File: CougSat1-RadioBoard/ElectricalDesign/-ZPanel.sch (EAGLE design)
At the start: 47 parts, among them J1 High Gain Antenna, J2 Deployables, J3 High Gain +, J4 ADCS, J5 Flap +X, J6 Flap -X, J7 Flap +Y, J8 Flap -Y, U1 AD7291, U3 AD8515

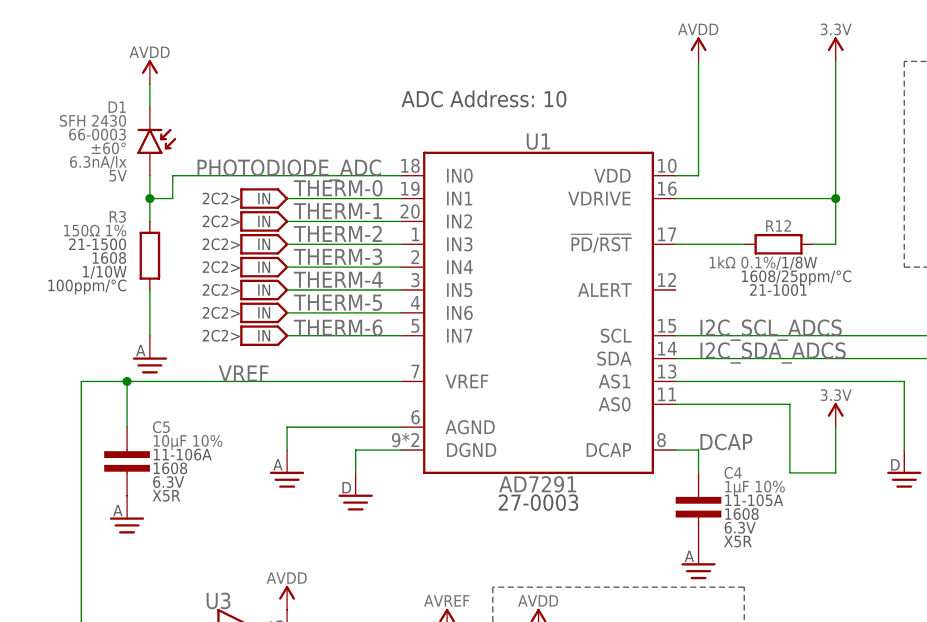
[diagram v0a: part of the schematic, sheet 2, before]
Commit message: Ready for re-review
Fixed issues mentioned before.
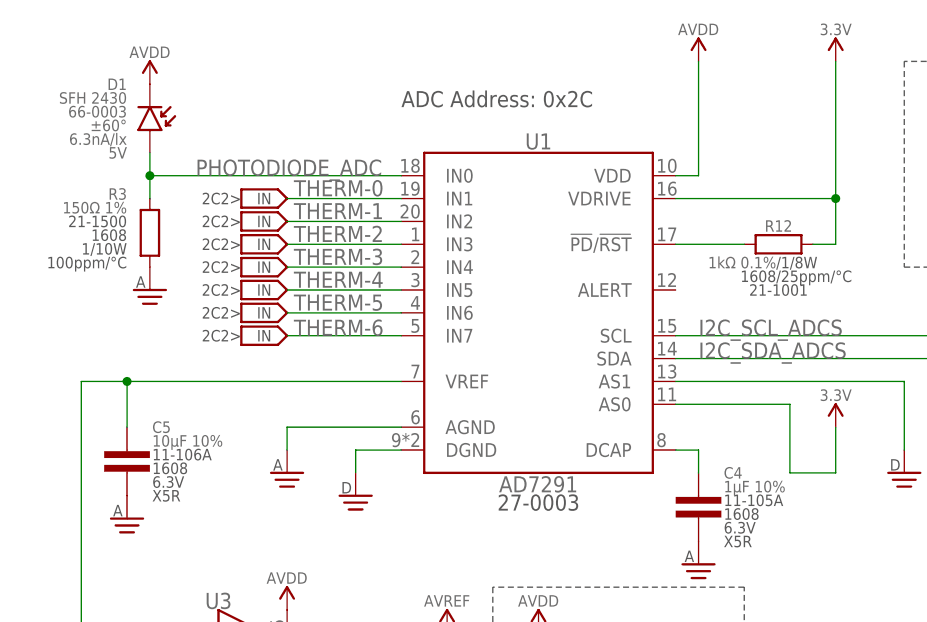
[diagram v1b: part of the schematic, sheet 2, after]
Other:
- note added: "ADC Address: 0x2C"
- note removed: "ADC Address: 10"
- moved on the sheet: D1, R3
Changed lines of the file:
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@@
 <wire x1="78.74" y1="106.68" x2="78.74" y2="129.54" width="0.1524" layer="97" style="shortdash"/>
 <wire x1="78.74" y1="129.54" x2="50.8" y2="129.54" width="0.1524" layer="97" style="shortdash"/>
-<text x="40.64" y="182.88" size="1.778" layer="97">ADC Address: 10</text>
+<text x="40.64" y="182.88" size="1.778" layer="97">ADC Address: 0x2C</text>
 </plain>
 <instances>
@@
 <attribute name="PACKAGE" x="11.557" y="63.754" size="1.778" layer="97" align="center"/>
 </instance>
-<instance part="D1" gate="G$1" x="12.7" y="180.34" smashed="yes" rot="R180">
-<attribute name="NAME" x="10.16" y="182.88" size="1.27" layer="95" rot="R180" align="center-left"/>
-<attribute name="VALUE" x="10.16" y="181.356" size="1.27" layer="95" rot="R180" align="center-left"/>
-<attribute name="SKU" x="10.16" y="179.832" size="1.27" layer="95" rot="R180" align="center-left"/>
-<attribute name="SENSITIVITY" x="10.16" y="176.784" size="1.27" layer="95" rot="R180" align="center-left"/>
-<attribute name="VR" x="10.16" y="175.26" size="1.27" layer="95" rot="R180" align="center-left"/>
-<attribute name="HALF_ANGLE" x="10.16" y="178.308" size="1.27" layer="95" rot="R180" align="center-left"/>
-</instance>
-<instance part="R3" gate="G$1" x="12.7" y="165.1" smashed="yes" rot="MR0">
-<attribute name="NAME" x="10.16" y="170.688" size="1.27" layer="95" rot="MR0" align="center-left"/>
-<attribute name="VALUE" x="10.16" y="169.164" size="1.27" layer="96" rot="MR0" align="center-left"/>
-<attribute name="PACKAGE" x="10.16" y="166.116" size="1.27" layer="97" rot="MR0" align="center-left"/>
-<attribute name="POWER" x="10.16" y="164.592" size="1.27" layer="97" rot="MR0" align="center-left"/>
-<attribute name="TEMP" x="10.16" y="163.068" size="1.27" layer="97" rot="MR0" align="center-left"/>
-<attribute name="SKU" x="10.16" y="167.64" size="1.27" layer="97" rot="MR0" align="center-left"/>
-</instance>
-<instance part="SUPPLY1" gate="G$1" x="12.7" y="154.94" smashed="yes"/>
+<instance part="D1" gate="G$1" x="12.7" y="182.88" smashed="yes" rot="R180">
+<attribute name="NAME" x="10.16" y="185.42" size="1.27" layer="95" rot="R180" align="center-left"/>
+<attribute name="VALUE" x="10.16" y="183.896" size="1.27" layer="95" rot="R180" align="center-left"/>
+<attribute name="SKU" x="10.16" y="182.372" size="1.27" layer="95" rot="R180" align="center-left"/>
+<attribute name="SENSITIVITY" x="10.16" y="179.324" size="1.27" layer="95" rot="R180" align="center-left"/>
+<attribute name="VR" x="10.16" y="177.8" size="1.27" layer="95" rot="R180" align="center-left"/>
+<attribute name="HALF_ANGLE" x="10.16" y="180.848" size="1.27" layer="95" rot="R180" align="center-left"/>
+</instance>
+<instance part="R3" gate="G$1" x="12.7" y="167.64" smashed="yes" rot="MR0">
+<attribute name="NAME" x="10.16" y="173.228" size="1.27" layer="95" rot="MR0" align="center-left"/>
+<attribute name="VALUE" x="10.16" y="171.704" size="1.27" layer="96" rot="MR0" align="center-left"/>
+<attribute name="PACKAGE" x="10.16" y="168.656" size="1.27" layer="97" rot="MR0" align="center-left"/>
+<attribute name="POWER" x="10.16" y="167.132" size="1.27" layer="97" rot="MR0" align="center-left"/>
+<attribute name="TEMP" x="10.16" y="165.608" size="1.27" layer="97" rot="MR0" align="center-left"/>
+<attribute name="SKU" x="10.16" y="170.18" size="1.27" layer="97" rot="MR0" align="center-left"/>
+</instance>
+<instance part="SUPPLY1" gate="G$1" x="12.7" y="162.56" smashed="yes"/>
 <instance part="J3" gate="G$1" x="190.5" y="177.8" smashed="yes">
 <attribute name="VALUE" x="191.135" y="173.99" size="1.778" layer="96" align="center"/>
@@
 </net>
 <net name="AGND" class="0">
-<segment>
-<pinref part="R3" gate="G$1" pin="1"/>
-<wire x1="12.7" y1="162.56" x2="12.7" y2="157.48" width="0.1524" layer="91"/>
-<pinref part="SUPPLY1" gate="G$1" pin="AGND"/>
-</segment>
 <segment>
 <pinref part="SUPPLY16" gate="G$1" pin="AGND"/>
@@
 <pinref part="SUPPLY42" gate="G$1" pin="AGND"/>
 </segment>
+<segment>
+<pinref part="R3" gate="G$1" pin="1"/>
+<pinref part="SUPPLY1" gate="G$1" pin="AGND"/>
+</segment>
 </net>
 <net name="3.3V" class="0">
@@
 <segment>
 <pinref part="D1" gate="G$1" pin="C"/>
-<wire x1="12.7" y1="182.88" x2="12.7" y2="185.42" width="0.1524" layer="91"/>
 <pinref part="SUPPLY2" gate="G$1" pin="AVDD"/>
 </segment>
@@
 <wire x1="73.66" y1="142.24" x2="73.66" y2="144.78" width="0.1524" layer="91"/>
 <wire x1="73.66" y1="144.78" x2="71.12" y2="144.78" width="0.1524" layer="91"/>
-<label x="73.66" y="144.78" size="1.778" layer="95"/>
 </segment>
 </net>
@@
 <wire x1="10.16" y1="147.32" x2="10.16" y2="152.4" width="0.1524" layer="91"/>
 <junction x="10.16" y="152.4"/>
-<label x="20.32" y="152.4" size="1.778" layer="95"/>
 </segment>
 </net>
@@
 <segment>
 <pinref part="U1" gate="G$1" pin="IN0"/>
-<wire x1="40.64" y1="175.26" x2="15.24" y2="175.26" width="0.1524" layer="91"/>
-<wire x1="15.24" y1="175.26" x2="15.24" y2="172.72" width="0.1524" layer="91"/>
+<wire x1="40.64" y1="175.26" x2="12.7" y2="175.26" width="0.1524" layer="91"/>
+<label x="17.78" y="175.26" size="1.778" layer="95"/>
+<pinref part="D1" gate="G$1" pin="A"/>
 <pinref part="R3" gate="G$1" pin="2"/>
-<pinref part="D1" gate="G$1" pin="A"/>
-<wire x1="12.7" y1="170.18" x2="12.7" y2="172.72" width="0.1524" layer="91"/>
 <wire x1="12.7" y1="172.72" x2="12.7" y2="175.26" width="0.1524" layer="91"/>
-<wire x1="15.24" y1="172.72" x2="12.7" y2="172.72" width="0.1524" layer="91"/>
-<junction x="12.7" y="172.72"/>
-<label x="17.78" y="175.26" size="1.778" layer="95"/>
-</segment>
-</net>
+<wire x1="12.7" y1="175.26" x2="12.7" y2="177.8" width="0.1524" layer="91"/>
+<junction x="12.7" y="175.26"/>
+</segment>
+</net>

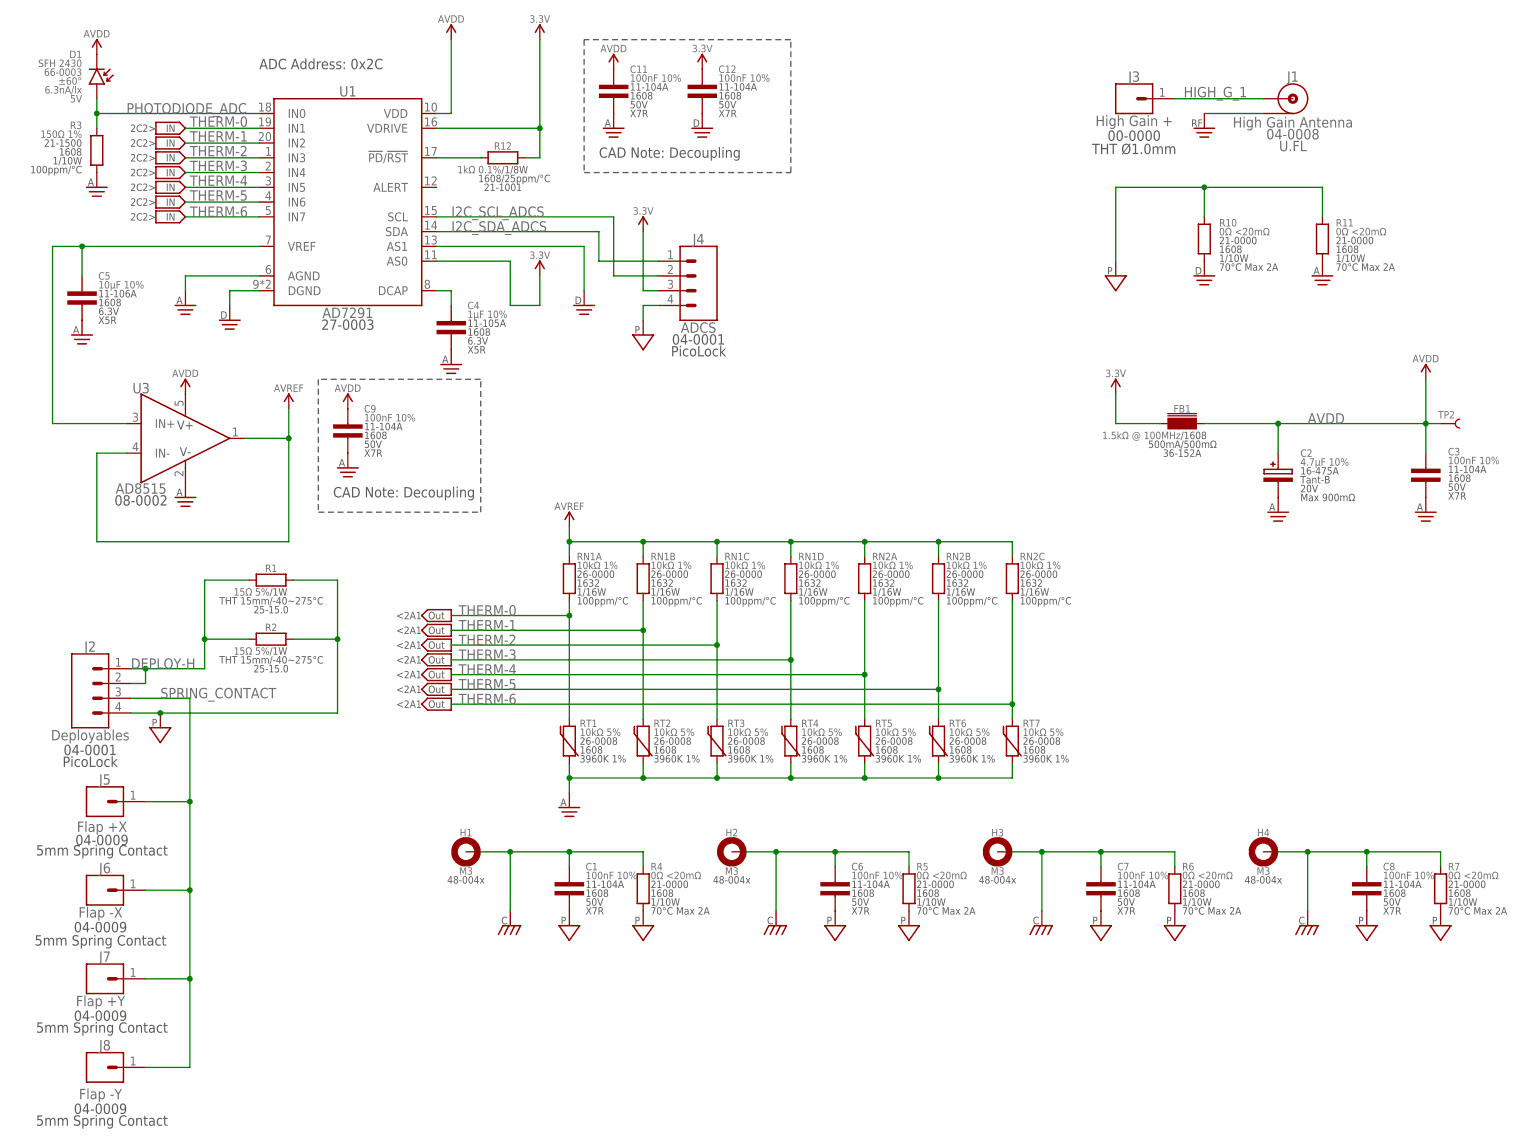
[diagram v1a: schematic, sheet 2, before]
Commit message: Fixed formatting and adjusted antenna tests
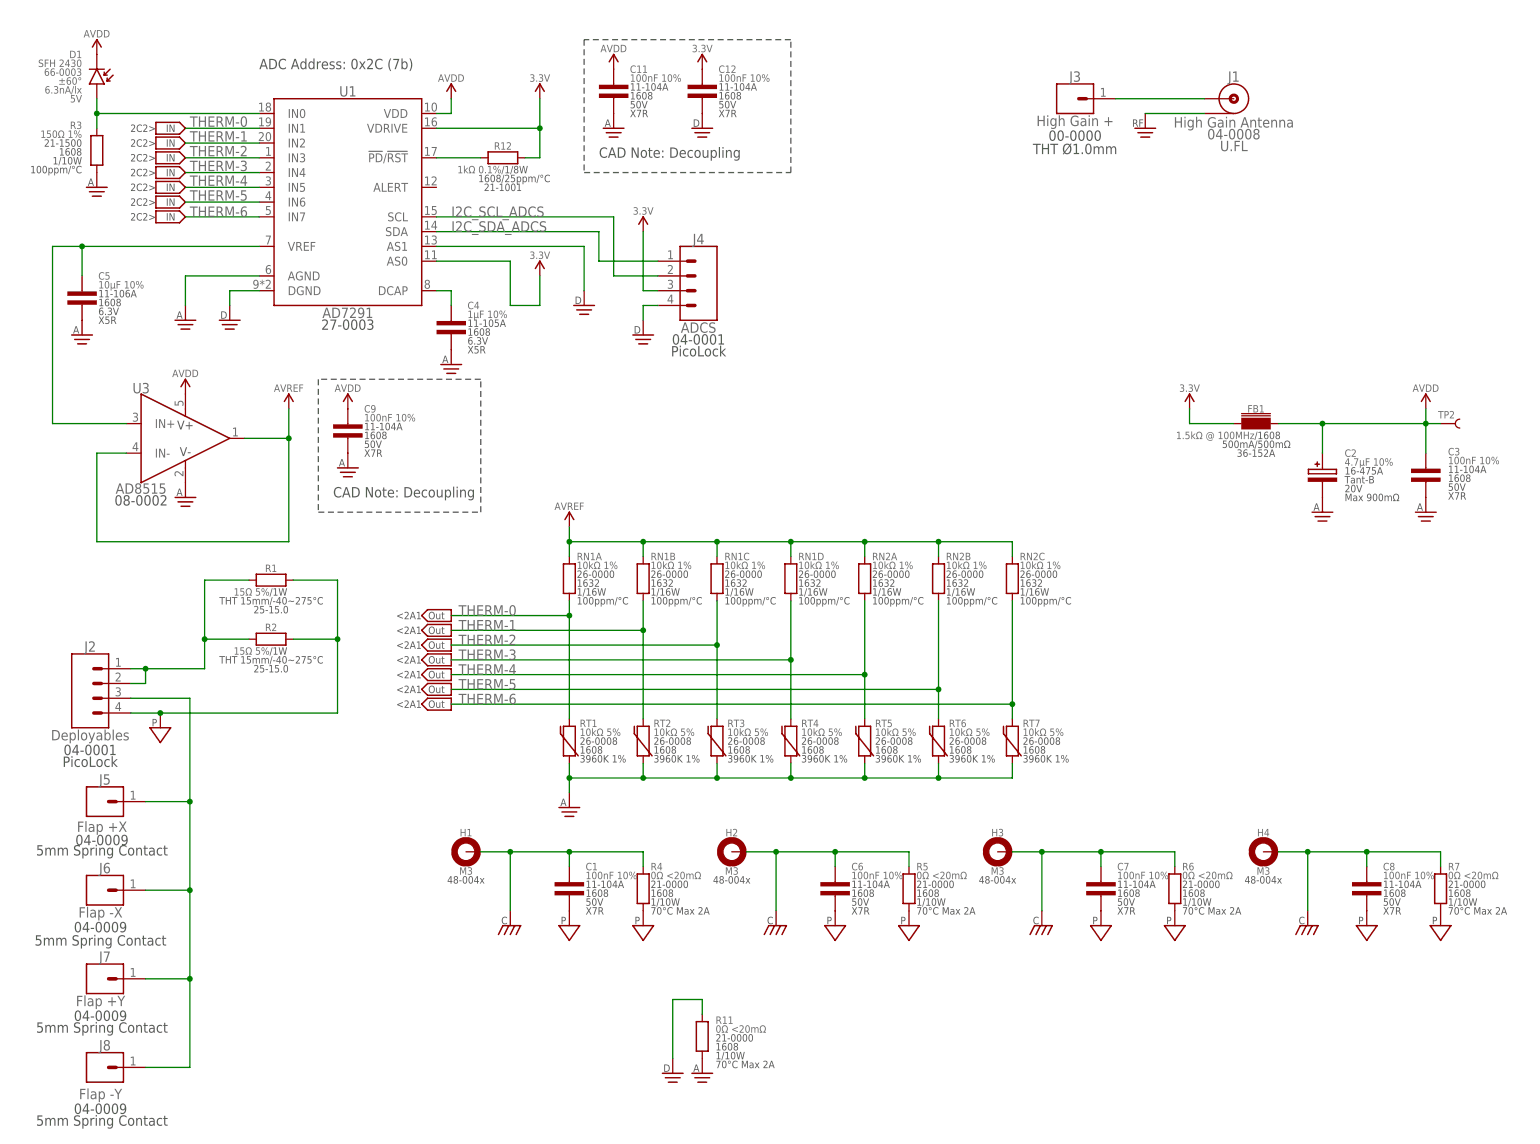
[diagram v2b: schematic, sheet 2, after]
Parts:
- removed R10: 0Ω <20mΩ, CougsInSpace-Resistors:RES-V-0-1608
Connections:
- net DGND: now also J4.4, R11.2; no longer R10.1
- net PGND: no longer J4.4, R10.2, R11.2
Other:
- note added: "ADC Address: 0x2C (7b)"
- note added: "Page 1: Block Diagram Page 2: Schematic Page 3: Mechanical"
- note added: "Photodiode"
- note removed: "96mm"
- note removed: "ADC Address: 0x2C"
- note removed: "CAD Note: Center Point"
- note removed: "Page 1: Block Diagram Page 2: Electrical Schematic Page 3: Mechanical"
- note removed: "Photodiodes"
- moved on the sheet: C2, FB1, J1, J3, R11

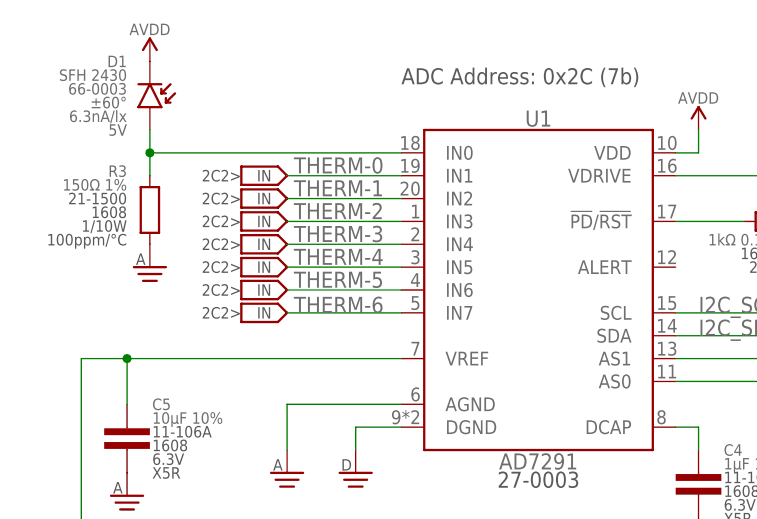
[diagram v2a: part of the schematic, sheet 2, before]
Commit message: Layout 1.0.1
Layout is ready for review. I changed the order of thermal inputs to the ADC for layout purposes on the schematic side also
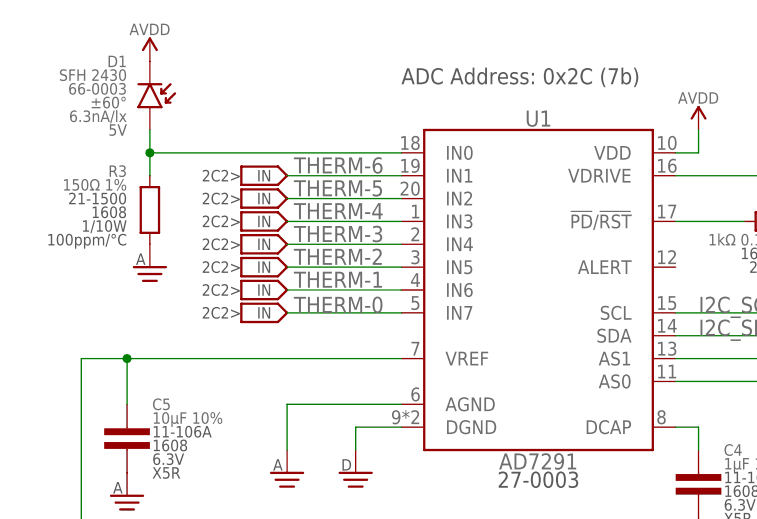
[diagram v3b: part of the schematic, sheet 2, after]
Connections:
- net THERM-0: now also U1.IN7; no longer U1.IN1
- net THERM-1: now also U1.IN6; no longer U1.IN2
- net THERM-2: now also U1.IN5; no longer U1.IN3
- net THERM-4: now also U1.IN3; no longer U1.IN5
- net THERM-5: now also U1.IN2; no longer U1.IN6
- net THERM-6: now also U1.IN1; no longer U1.IN7
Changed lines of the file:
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@@
 <?xml version="1.0" encoding="utf-8"?>
 <!DOCTYPE eagle SYSTEM "eagle.dtd">
-<eagle version="9.5.1">
+<eagle version="9.5.2">
 <drawing>
 <settings>
@@
 </segment>
 <segment>
-<pinref part="U1" gate="G$1" pin="IN1"/>
-<wire x1="40.64" y1="172.72" x2="27.94" y2="172.72" width="0.1524" layer="91"/>
-<label x="28.702" y="172.974" size="1.778" layer="95"/>
+<pinref part="U1" gate="G$1" pin="IN7"/>
+<wire x1="40.64" y1="157.48" x2="27.94" y2="157.48" width="0.1524" layer="91"/>
+<label x="28.702" y="157.48" size="1.778" layer="95"/>
 </segment>
 </net>
@@
 </segment>
 <segment>
-<pinref part="U1" gate="G$1" pin="IN2"/>
-<wire x1="40.64" y1="170.18" x2="27.94" y2="170.18" width="0.1524" layer="91"/>
-<label x="28.702" y="170.434" size="1.778" layer="95"/>
+<pinref part="U1" gate="G$1" pin="IN6"/>
+<wire x1="40.64" y1="160.02" x2="27.94" y2="160.02" width="0.1524" layer="91"/>
+<label x="28.702" y="160.274" size="1.778" layer="95"/>
 </segment>
 </net>
@@
 </segment>
 <segment>
-<pinref part="U1" gate="G$1" pin="IN3"/>
-<wire x1="40.64" y1="167.64" x2="27.94" y2="167.64" width="0.1524" layer="91"/>
-<label x="28.702" y="167.894" size="1.778" layer="95"/>
+<pinref part="U1" gate="G$1" pin="IN5"/>
+<wire x1="40.64" y1="162.56" x2="27.94" y2="162.56" width="0.1524" layer="91"/>
+<label x="28.702" y="162.814" size="1.778" layer="95"/>
 </segment>
 </net>
@@
 </segment>
 <segment>
-<pinref part="U1" gate="G$1" pin="IN5"/>
-<wire x1="40.64" y1="162.56" x2="27.94" y2="162.56" width="0.1524" layer="91"/>
-<label x="28.702" y="162.814" size="1.778" layer="95"/>
+<pinref part="U1" gate="G$1" pin="IN3"/>
+<wire x1="40.64" y1="167.64" x2="27.94" y2="167.64" width="0.1524" layer="91"/>
+<label x="28.702" y="167.894" size="1.778" layer="95"/>
 </segment>
 </net>
@@
 </segment>
 <segment>
-<pinref part="U1" gate="G$1" pin="IN6"/>
-<wire x1="40.64" y1="160.02" x2="27.94" y2="160.02" width="0.1524" layer="91"/>
-<label x="28.702" y="160.274" size="1.778" layer="95"/>
+<pinref part="U1" gate="G$1" pin="IN2"/>
+<wire x1="40.64" y1="170.18" x2="27.94" y2="170.18" width="0.1524" layer="91"/>
+<label x="28.702" y="170.434" size="1.778" layer="95"/>
 </segment>
 </net>
@@
 </segment>
 <segment>
-<pinref part="U1" gate="G$1" pin="IN7"/>
-<wire x1="40.64" y1="157.48" x2="27.94" y2="157.48" width="0.1524" layer="91"/>
-<label x="28.702" y="157.48" size="1.778" layer="95"/>
-</segment>
-</net>
+<pinref part="U1" gate="G$1" pin="IN1"/>
+<wire x1="40.64" y1="172.72" x2="27.94" y2="172.72" width="0.1524" layer="91"/>
+<label x="28.702" y="172.974" size="1.778" layer="95"/>
+</segment>
+</net>

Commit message: Layout 1.0.2
Ready for RF
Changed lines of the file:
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@@
 <pinref part="D1" gate="G$1" pin="C"/>
 <pinref part="SUPPLY2" gate="G$1" pin="AVDD"/>
+<wire x1="12.7" y1="185.42" x2="12.7" y2="177.8" width="0.1524" layer="91"/>
 </segment>
 <segment>
@@
 <pinref part="R3" gate="G$1" pin="2"/>
 <wire x1="12.7" y1="172.72" x2="12.7" y2="175.26" width="0.1524" layer="91"/>
-<wire x1="12.7" y1="175.26" x2="12.7" y2="177.8" width="0.1524" layer="91"/>
+<wire x1="12.7" y1="175.26" x2="12.7" y2="185.42" width="0.1524" layer="91"/>
 <junction x="12.7" y="175.26"/>
 </segment>
